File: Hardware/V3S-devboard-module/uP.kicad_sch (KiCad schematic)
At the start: 29 parts, among them J101 Micro_SD_Card_Det1, SW101 SW_MEC_5E, U102 W25Q128JVS, U201 V3S, Y1 Crystal_GND23_Small, Y2 Crystal_GND23_Small

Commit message: minor improvements and fixes
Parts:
- C235: value 18p -> 100n
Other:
- moved on the sheet: R216, R217
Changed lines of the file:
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@@
 	)
 	(bus_entry
-		(at 200.66 35.56)
+		(at 171.45 39.37)
 		(size -2.54 2.54)
 		(stroke
@@
 	)
 	(bus_entry
-		(at 162.56 35.56)
+		(at 133.35 39.37)
 		(size 2.54 2.54)
 		(stroke
@@
 	)
 	(bus_entry
-		(at 162.56 33.02)
+		(at 133.35 36.83)
 		(size 2.54 2.54)
 		(stroke
@@
 	)
 	(bus_entry
-		(at 200.66 33.02)
+		(at 171.45 36.83)
 		(size -2.54 2.54)
 		(stroke
@@
 	(wire
 		(pts
-			(xy 181.61 35.56) (xy 198.12 35.56)
+			(xy 152.4 39.37) (xy 168.91 39.37)
 		)
 		(stroke
@@
 	(bus
 		(pts
-			(xy 161.29 31.75) (xy 162.56 33.02)
+			(xy 132.08 35.56) (xy 133.35 36.83)
 		)
 		(stroke
@@
 	(wire
 		(pts
-			(xy 165.1 35.56) (xy 176.53 35.56)
+			(xy 135.89 39.37) (xy 147.32 39.37)
 		)
 		(stroke
@@
 	(wire
 		(pts
-			(xy 165.1 38.1) (xy 181.61 38.1)
+			(xy 135.89 41.91) (xy 152.4 41.91)
 		)
 		(stroke
@@
 	(bus
 		(pts
-			(xy 201.93 31.75) (xy 217.17 31.75)
+			(xy 172.72 35.56) (xy 187.96 35.56)
 		)
 		(stroke
@@
 	(wire
 		(pts
-			(xy 186.69 38.1) (xy 198.12 38.1)
+			(xy 157.48 41.91) (xy 168.91 41.91)
 		)
 		(stroke
@@
 	(bus
 		(pts
-			(xy 200.66 33.02) (xy 200.66 35.56)
+			(xy 171.45 36.83) (xy 171.45 39.37)
 		)
 		(stroke
@@
 	(bus
 		(pts
-			(xy 200.66 33.02) (xy 201.93 31.75)
+			(xy 171.45 36.83) (xy 172.72 35.56)
 		)
 		(stroke
@@
 	(bus
 		(pts
-			(xy 162.56 33.02) (xy 162.56 35.56)
+			(xy 133.35 36.83) (xy 133.35 39.37)
 		)
 		(stroke
@@
 	(bus
 		(pts
-			(xy 161.29 31.75) (xy 151.13 31.75)
+			(xy 132.08 35.56) (xy 121.92 35.56)
 		)
 		(stroke
@@
 	)
 	(label "SDC0.CLK"
-		(at 175.26 35.56 180)
+		(at 146.05 39.37 180)
 		(effects
 			(font
@@
 	)
 	(label "SDC0.D3"
-		(at 173.99 38.1 180)
+		(at 144.78 41.91 180)
 		(effects
 			(font
@@
 	)
 	(label "UART0{UART}"
-		(at 217.17 31.75 180)
+		(at 187.96 35.56 180)
 		(fields_autoplaced yes)
 		(effects
@@
 	)
 	(label "UART0.TX"
-		(at 198.12 35.56 180)
+		(at 168.91 39.37 180)
 		(fields_autoplaced yes)
 		(effects
@@
 	)
 	(label "UART0.RX"
-		(at 198.12 38.1 180)
+		(at 168.91 41.91 180)
 		(fields_autoplaced yes)
 		(effects
@@
 	)
 	(label "SDC0{SDC}"
-		(at 151.13 31.75 0)
+		(at 121.92 35.56 0)
 		(fields_autoplaced yes)
 		(effects
@@
 			)
 		)
-		(property "Value" "18p"
+		(property "Value" "100n"
 			(at 382.016 141.732 0)
 			(effects
@@
 	(symbol
 		(lib_id "Device:R_Small_US")
-		(at 179.07 35.56 90)
+		(at 149.86 39.37 90)
 		(unit 1)
 		(exclude_from_sim no)
@@
 		(dnp yes)
 		(property "Reference" "R216"
-			(at 180.34 32.766 90)
+			(at 151.13 36.576 90)
 			(effects
 				(font
@@
 		)
 		(property "Value" "33"
-			(at 183.896 32.766 90)
+			(at 154.686 36.576 90)
 			(effects
 				(font
@@
 		)
 		(property "Footprint" "Resistor_SMD:R_0603_1608Metric"
-			(at 179.07 35.56 0)
+			(at 149.86 39.37 0)
 			(effects
 				(font
@@
 		)
 		(property "Datasheet" "~"
-			(at 179.07 35.56 0)
+			(at 149.86 39.37 0)
 			(effects
 				(font
@@
 		)
 		(property "Description" "Resistor, small US symbol"
-			(at 179.07 35.56 0)
+			(at 149.86 39.37 0)
 			(effects
 				(font
@@
 		)
 		(property "Precision" ""
-			(at 183.388 37.846 90)
+			(at 154.178 41.656 90)
 			(effects
 				(font
@@
 	(symbol
 		(lib_id "Device:R_Small_US")
-		(at 184.15 38.1 90)
+		(at 154.94 41.91 90)
 		(unit 1)
 		(exclude_from_sim no)
@@
 		(dnp yes)
 		(property "Reference" "R217"
-			(at 185.166 40.894 90)
+			(at 155.956 44.704 90)
 			(effects
 				(font
@@
 		)
 		(property "Value" "33"
-			(at 188.976 41.148 90)
+			(at 159.766 44.958 90)
 			(effects
 				(font
@@
 		)
 		(property "Footprint" "Resistor_SMD:R_0603_1608Metric"
-			(at 184.15 38.1 0)
+			(at 154.94 41.91 0)
 			(effects
 				(font
@@
 		)
 		(property "Datasheet" "~"
-			(at 184.15 38.1 0)
+			(at 154.94 41.91 0)
 			(effects
 				(font
@@
 		)
 		(property "Description" "Resistor, small US symbol"
-			(at 184.15 38.1 0)
+			(at 154.94 41.91 0)
 			(effects
 				(font
@@
 		)
 		(property "Precision" ""
-			(at 188.468 40.386 90)
+			(at 159.258 44.196 90)
 			(effects
 				(font

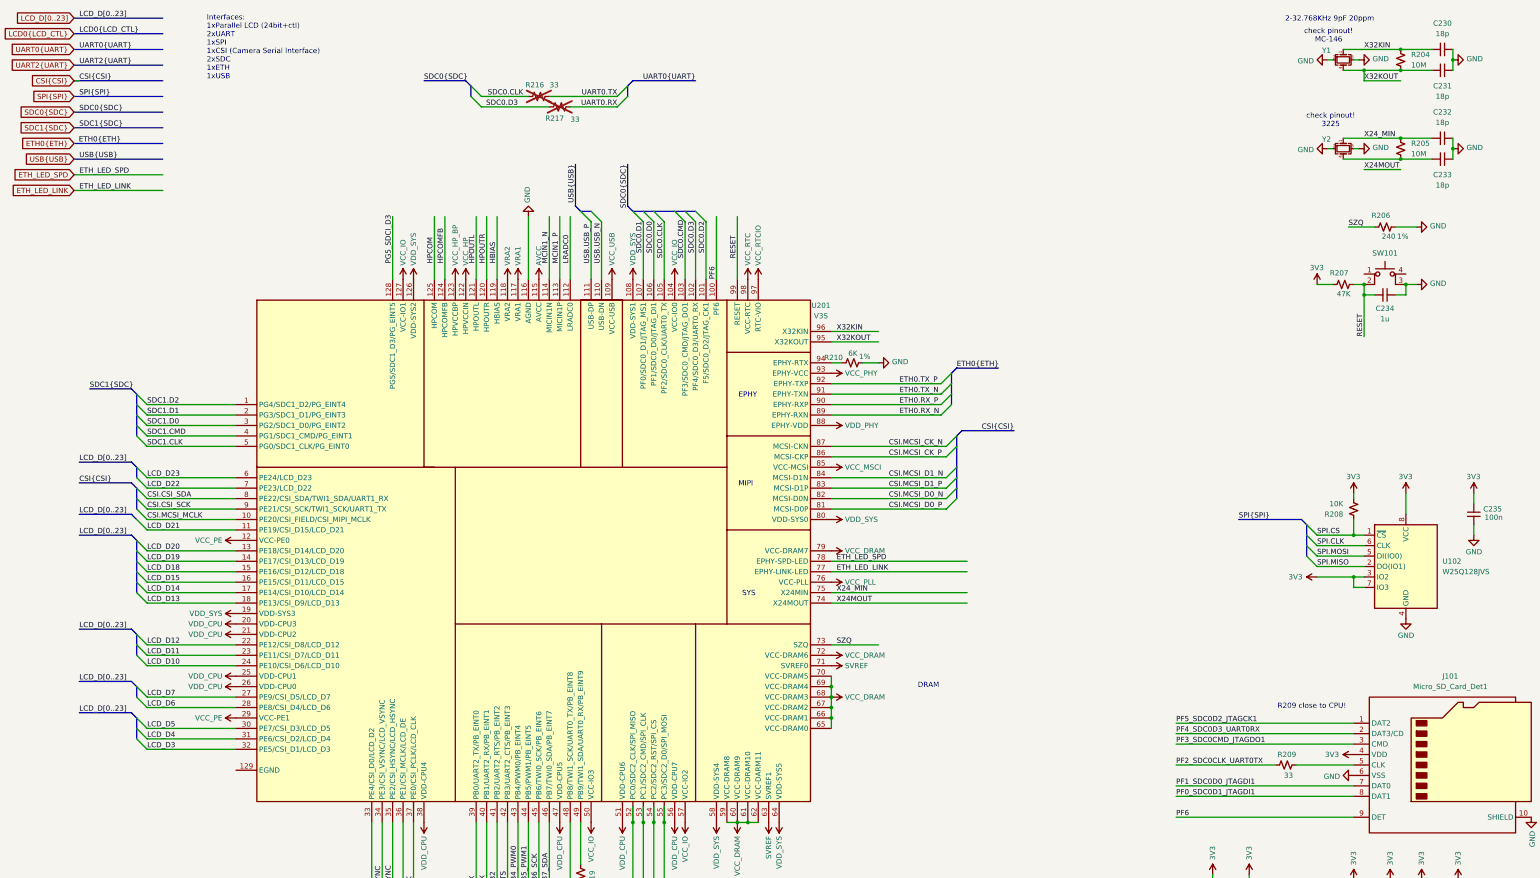
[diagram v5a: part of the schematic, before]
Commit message: fixed minor schematic issues
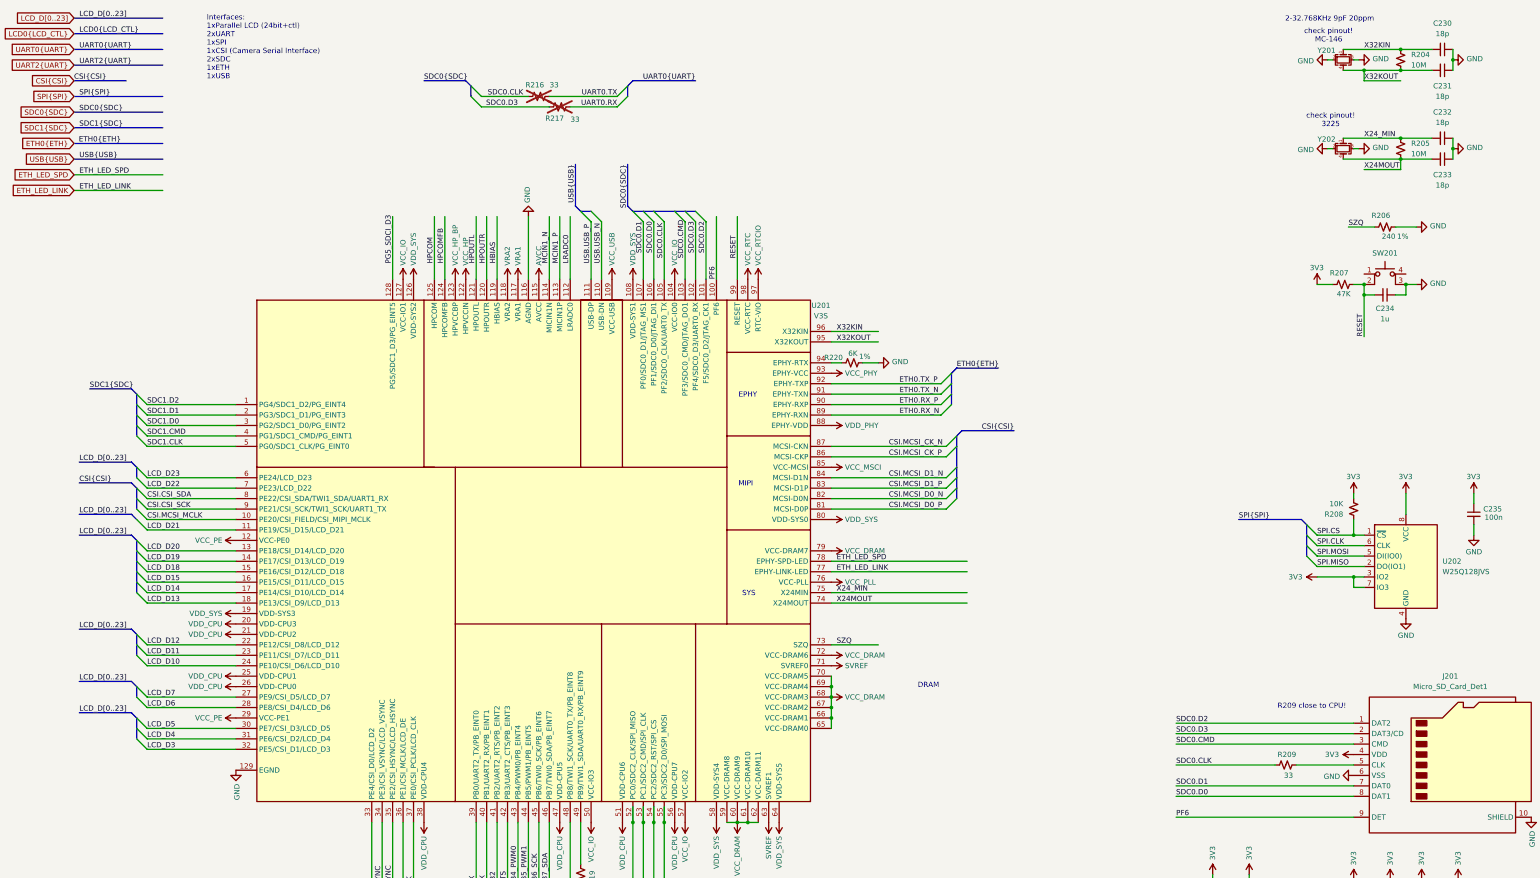
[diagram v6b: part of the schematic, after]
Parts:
- R220: renamed from R210; footprint (none) -> Resistor_SMD:R_0603_1608Metric
- SW201: renamed from SW101; footprint mod:SW_SKRPACE010 -> v3s-devboard-module:SW_SKRPACE010
- Y201: renamed from Y1; footprint (none) -> Crystal:Crystal_SMD_3225-4Pin_3.2x2.5mm
- renumbered J101 to J201, U102 to U202, Y2 to Y202
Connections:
- net PF2_SDC0CLK_UART0TX is gone; now on net SDC0.CLK: R209.1
- net GND: now also U201.129 (EGND)
- net PF0_SDC0D1_JTAGDI1: no longer J201.8 (DAT1)
- net PF1_SDC0D0_JTAGDI1: no longer J201.7 (DAT0)
- net PF3_SDC0CMD_JTAGDO1: no longer J201.3 (CMD)
- net PF4_SDC0D3_UART0RX: no longer J201.2 (DAT3/CD)
- net PF5_SDC0D2_JTAGCK1: no longer J201.1 (DAT2)
- net SDC0.CMD: now also J201.3 (CMD)
- net SDC0.D0: now also J201.8 (DAT1)
- net SDC0.D1: now also J201.7 (DAT0)
- net SDC0.D2: now also J201.1 (DAT2)
- net SDC0.D3: now also J201.2 (DAT3/CD)
- net X24MOUT: now also C233.2, R205.2, Y202.4

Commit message: started preparing layout
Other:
- note added: "check pinout! 3225 CRY-TSX3225"
- note added: "check pinout! MC-146 32768"
- note removed: "check pinout! 3225"
- note removed: "check pinout! MC-146"
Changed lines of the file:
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@@
 		)
 	)
-	(text "check pinout!\n3225"
+	(text "check pinout!\n3225\nCRY-TSX3225"
 		(exclude_from_sim no)
 		(at 342.392 45.212 0)
@@
 		)
 	)
-	(text "check pinout!\nMC-146"
+	(text "check pinout!\nMC-146\n32768"
 		(exclude_from_sim no)
 		(at 341.884 24.638 0)

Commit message: small layout
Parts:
- removed Y201, Y202: Crystal_GND23_Small, Crystal:Crystal_SMD_3225-4Pin_3.2x2.5mm, symbol Device:Crystal_GND23_Small
- added Y201, Y202: Crystal_GND24_Small, Crystal:Crystal_SMD_2520-4Pin_2.5x2.0mm, symbol Device:Crystal_GND24_Small
- C230, C231, C232, C233: footprint Capacitor_SMD:C_0603_1608Metric -> Capacitor_SMD:C_0402_1005Metric
- R204, R205, R206: footprint Resistor_SMD:R_0603_1608Metric -> Resistor_SMD:R_0402_1005Metric
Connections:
- net GND: now also Y201.2, Y201.4, Y202.2, Y202.4
- net PF6: no longer U201.100 (PF6)
- net X24MOUT: now also Y202.3
- net X24_MIN: now also Y202.1
- net X32KIN: now also Y201.1
- net X32KOUT: now also Y201.3
- new net USB.USB_ID: U201.100 (PF6)
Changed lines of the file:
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@@
 	)
 	(bus_alias "USB"
-		(members "USB_P" "USB_N")
+		(members "USB_P" "USB_N" "USB_ID")
 	)
 	(junction
@@
 	)
 	(bus_entry
+		(at 190.5 68.58)
+		(size 2.54 2.54)
+		(stroke
+			(width 0)
+			(type default)
+		)
+	)
+	(bus_entry
 		(at 251.46 137.16)
 		(size -2.54 2.54)
@@
 	(bus
 		(pts
+			(xy 189.23 67.31) (xy 189.23 57.15)
+		)
+		(stroke
+			(width 0)
+			(type default)
+		)
+	)
+	(bus
+		(pts
 			(xy 168.91 241.3) (xy 170.18 240.03)
 		)
@@
 	(wire
 		(pts
+			(xy 193.04 71.12) (xy 193.04 83.82)
+		)
+		(stroke
+			(width 0)
+			(type default)
+		)
+	)
+	(wire
+		(pts
 			(xy 54.61 172.72) (xy 76.2 172.72)
 		)
@@
 	(bus
 		(pts
+			(xy 189.23 67.31) (xy 190.5 68.58)
+		)
+		(stroke
+			(width 0)
+			(type default)
+		)
+	)
+	(bus
+		(pts
 			(xy 50.8 168.91) (xy 52.07 170.18)
 		)
@@
 	(wire
 		(pts
-			(xy 193.04 83.82) (xy 193.04 68.58)
-		)
-		(stroke
-			(width 0)
-			(type default)
-		)
-	)
-	(wire
-		(pts
 			(xy 147.32 215.9) (xy 147.32 231.14)
 		)
@@
 		)
 	)
+	(label "USB{USB}"
+		(at 189.23 57.15 270)
+		(fields_autoplaced yes)
+		(effects
+			(font
+				(size 1.27 1.27)
+			)
+			(justify right bottom)
+		)
+	)
 	(label "SDC0.CLK"
 		(at 146.05 39.37 180)
@@
 		)
 	)
-	(label "PF6"
-		(at 193.04 83.82 90)
-		(fields_autoplaced yes)
-		(effects
-			(font
-				(size 1.27 1.27)
-			)
-			(justify left bottom)
-		)
-	)
 	(label "X32KIN"
 		(at 350.52 27.94 0)
@@
 		)
 	)
+	(label "USB.USB_ID"
+		(at 193.04 83.82 90)
+		(fields_autoplaced yes)
+		(effects
+			(font
+				(size 1.27 1.27)
+			)
+			(justify left bottom)
+		)
+	)
 	(label "LCD_D22"
 		(at 54.61 134.62 0)
@@
 	)
 	(symbol
+		(lib_id "Device:Crystal_GND24_Small")
+		(at 345.44 52.07 270)
+		(unit 1)
+		(exclude_from_sim no)
+		(in_bom yes)
+		(on_board yes)
+		(dnp no)
+		(property "Reference" "Y202"
+			(at 342.646 55.372 90)
+			(effects
+				(font
+					(size 1.27 1.27)
+				)
+			)
+		)
+		(property "Value" "Crystal_GND24_Small"
+			(at 340.868 51.816 0)
+			(effects
+				(font
+					(size 1.27 1.27)
+				)
+				(hide yes)
+			)
+		)
+		(property "Footprint" "Crystal:Crystal_SMD_2520-4Pin_2.5x2.0mm"
+			(at 345.44 52.07 0)
+			(effects
+				(font
+					(size 1.27 1.27)
+				)
+				(hide yes)
+			)
+		)
+		(property "Datasheet" "~"
+			(at 345.44 52.07 0)
+			(effects
+				(font
+					(size 1.27 1.27)
+				)
+				(hide yes)
+			)
+		)
+		(property "Description" "Four pin crystal, GND on pins 2 and 4, small symbol"
+			(at 345.44 52.07 0)
+			(effects
+				(font
+					(size 1.27 1.27)
+				)
+				(hide yes)
+			)
+		)
+		(pin "2"
+		)
+		(pin "1"
+		)
+		(pin "3"
+		)
+		(pin "4"
+		)
+		(instances
+			(project "V3S-devboard-module"
+				(path "/5d41c08e-2331-42df-a2d5-1aeb6ed4388c/f51f2d23-c28c-4ea4-895a-4b3207c38b48"
+					(reference "Y202")
+					(unit 1)
+				)
+			)
+		)
+	)
+	(symbol
 		(lib_id "power:VCC")
 		(at 220.98 149.86 270)
@@
 	)
 	(symbol
-		(lib_id "Device:Crystal_GND23_Small")
-		(at 345.44 52.07 270)
-		(unit 1)
-		(exclude_from_sim no)
-		(in_bom yes)
-		(on_board yes)
-		(dnp no)
-		(property "Reference" "Y202"
-			(at 341.376 49.784 90)
-			(effects
-				(font
-					(size 1.27 1.27)
-				)
-			)
-		)
-		(property "Value" "Crystal_GND23_Small"
-			(at 347.091 64.77 0)
-			(effects
-				(font
-					(size 1.27 1.27)
-				)
-				(hide yes)
-			)
-		)
-		(property "Footprint" "Crystal:Crystal_SMD_3225-4Pin_3.2x2.5mm"
-			(at 345.44 52.07 0)
-			(effects
-				(font
-					(size 1.27 1.27)
-				)
-				(hide yes)
-			)
-		)
-		(property "Datasheet" "~"
-			(at 345.44 52.07 0)
-			(effects
-				(font
-					(size 1.27 1.27)
-				)
-				(hide yes)
-			)
-		)
-		(property "Description" "Four pin crystal, GND on pins 2 and 3, small symbol"
-			(at 345.44 52.07 0)
-			(effects
-				(font
-					(size 1.27 1.27)
-				)
-				(hide yes)
-			)
-		)
-		(pin "4"
-		)
-		(pin "2"
-		)
-		(pin "1"
-		)
-		(pin "3"
-		)
-		(instances
-			(project "V3S-devboard-module"
-				(path "/5d41c08e-2331-42df-a2d5-1aeb6ed4388c/f51f2d23-c28c-4ea4-895a-4b3207c38b48"
-					(reference "Y202")
-					(unit 1)
-				)
-			)
-		)
-	)
-	(symbol
 		(lib_id "Device:R_Small_US")
 		(at 160.02 228.6 180)
@@
 			)
 		)
-		(property "Footprint" "Capacitor_SMD:C_0603_1608Metric"
+		(property "Footprint" "Capacitor_SMD:C_0402_1005Metric"
 			(at 369.57 54.61 0)
 			(effects
@@
 			)
 		)
-		(property "Footprint" "Resistor_SMD:R_0603_1608Metric"
+		(property "Footprint" "Resistor_SMD:R_0402_1005Metric"
 			(at 359.41 52.07 0)
 			(effects
@@
 			)
 		)
-		(property "Footprint" "Capacitor_SMD:C_0603_1608Metric"
+		(property "Footprint" "Capacitor_SMD:C_0402_1005Metric"
 			(at 369.57 27.94 0)
 			(effects
@@
 			)
 		)
-		(property "Footprint" "Capacitor_SMD:C_0603_1608Metric"
+		(property "Footprint" "Capacitor_SMD:C_0402_1005Metric"
 			(at 369.57 49.53 0)
 			(effects
@@
 	)
 	(symbol
+		(lib_id "Device:Crystal_GND24_Small")
+		(at 345.44 30.48 270)
+		(unit 1)
+		(exclude_from_sim no)
+		(in_bom yes)
+		(on_board yes)
+		(dnp no)
+		(property "Reference" "Y201"
+			(at 342.646 33.782 90)
+			(effects
+				(font
+					(size 1.27 1.27)
+				)
+			)
+		)
+		(property "Value" "Crystal_GND24_Small"
+			(at 340.868 30.226 0)
+			(effects
+				(font
+					(size 1.27 1.27)
+				)
+				(hide yes)
+			)
+		)
+		(property "Footprint" "Crystal:Crystal_SMD_2520-4Pin_2.5x2.0mm"
+			(at 345.44 30.48 0)
+			(effects
+				(font
+					(size 1.27 1.27)
+				)
+				(hide yes)
+			)
+		)
+		(property "Datasheet" "~"
+			(at 345.44 30.48 0)
+			(effects
+				(font
+					(size 1.27 1.27)
+				)
+				(hide yes)
+			)
+		)
+		(property "Description" "Four pin crystal, GND on pins 2 and 4, small symbol"
+			(at 345.44 30.48 0)
+			(effects
+				(font
+					(size 1.27 1.27)
+				)
+				(hide yes)
+			)
+		)
+		(pin "2"
+		)
+		(pin "1"
+		)
+		(pin "3"
+		)
+		(pin "4"
+		)
+		(instances
+			(project "V3S-devboard-module"
+				(path "/5d41c08e-2331-42df-a2d5-1aeb6ed4388c/f51f2d23-c28c-4ea4-895a-4b3207c38b48"
+					(reference "Y201")
+					(unit 1)
+				)
+			)
+		)
+	)
+	(symbol
 		(lib_id "power:VCC")
 		(at 339.09 156.21 90)
@@
 			)
 		)
-		(property "Footprint" "Capacitor_SMD:C_0603_1608Metric"
+		(property "Footprint" "Capacitor_SMD:C_0402_1005Metric"
 			(at 369.57 33.02 0)
 			(effects
@@
 			)
 		)
-		(property "Footprint" "Resistor_SMD:R_0603_1608Metric"
+		(property "Footprint" "Resistor_SMD:R_0402_1005Metric"
 			(at 359.41 30.48 0)
 			(effects
@@
 			)
 		)
-		(property "Footprint" "Resistor_SMD:R_0603_1608Metric"
+		(property "Footprint" "Resistor_SMD:R_0402_1005Metric"
 			(at 355.6 71.12 0)
 			(effects
@@
 					(unit 1)
 				)
-			)
-		)
-	)
-	(symbol
-		(lib_id "Device:Crystal_GND23_Small")
-		(at 345.44 30.48 270)
-		(unit 1)
-		(exclude_from_sim no)
-		(in_bom yes)
-		(on_board yes)
-		(dnp no)
-		(property "Reference" "Y201"
-			(at 341.376 28.194 90)
-			(effects
-				(font
-					(size 1.27 1.27)
-				)
-			)
-		)
-		(property "Value" "Crystal_GND23_Small"
-			(at 347.091 43.18 0)
-			(effects
-				(font
-					(size 1.27 1.27)
-				)
-				(hide yes)
-			)
-		)
-		(property "Footprint" "Crystal:Crystal_SMD_3225-4Pin_3.2x2.5mm"
-			(at 345.44 30.48 0)
-			(effects
-				(font
-					(size 1.27 1.27)
-				)
-				(hide yes)
-			)
-		)
-		(property "Datasheet" "~"
-			(at 345.44 30.48 0)
-			(effects
-				(font
-					(size 1.27 1.27)
-				)
-				(hide yes)
-			)
-		)
-		(property "Description" "Four pin crystal, GND on pins 2 and 3, small symbol"
-			(at 345.44 30.48 0)
-			(effects
-				(font
-					(size 1.27 1.27)
-				)
-				(hide yes)
-			)
-		)
-		(pin "4"
-		)
-		(pin "2"
-		)
-		(pin "1"
-		)
-		(pin "3"
-		)
-		(instances
-			(project "V3S-devboard-module"
-				(path "/5d41c08e-2331-42df-a2d5-1aeb6ed4388c/f51f2d23-c28c-4ea4-895a-4b3207c38b48"
-					(reference "Y201")
-					(unit 1)
-				)
